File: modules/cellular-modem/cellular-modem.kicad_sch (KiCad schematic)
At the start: 20 parts, among them J1 Bus_PCI_Express_Mini, U1 TXV0108RGYR, U2 TXV0108RGYR, U3 TXV0108RGYR, U4 TPS631000DRLR, U5 TPS631000DRLR

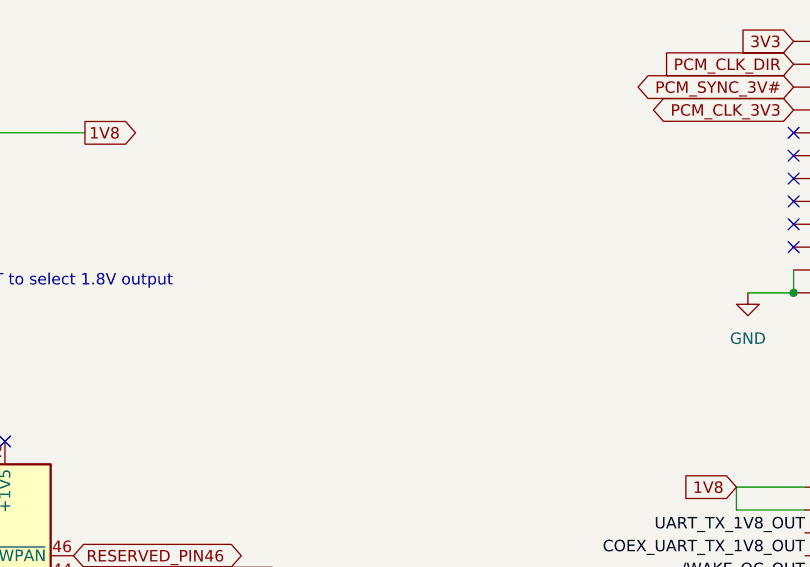
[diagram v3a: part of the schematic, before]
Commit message: add footprints etc for miniPCIe connector
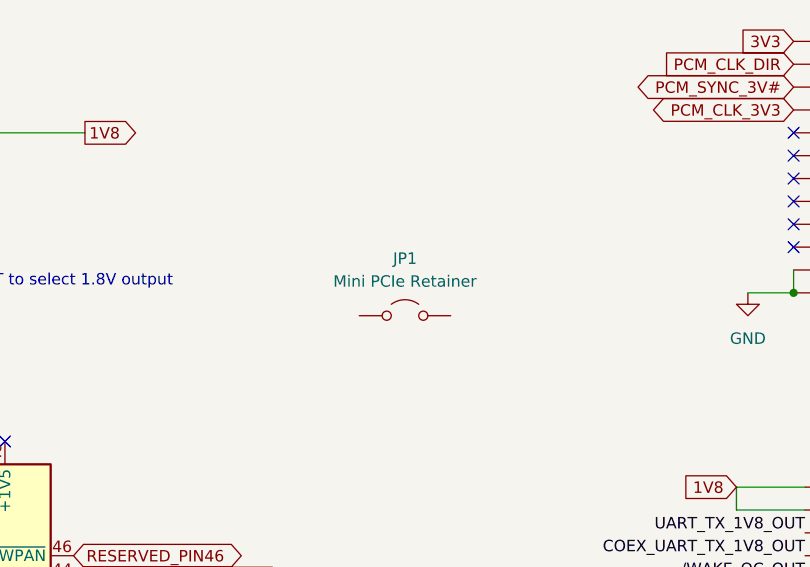
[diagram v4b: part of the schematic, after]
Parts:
- added JP1: Mini PCIe Retainer, cellular-modem:JAE_MM60-EZH059-B5-R650, symbol Jumper:Jumper_2_Open
- J1: footprint Connector_PCBEdge:BUS_PCI_Express_Mini_Dual -> cellular-modem:CONN_MM60-52B1-E1-R650_JAE
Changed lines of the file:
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@@
+	)
+	(symbol
+		(lib_id "Jumper:Jumper_2_Open")
+		(at 176.53 107.95 0)
+		(unit 1)
+		(exclude_from_sim yes)
+		(in_bom yes)
+		(on_board yes)
+		(dnp no)
+		(fields_autoplaced yes)
+		(property "Reference" "JP1"
+			(at 176.53 101.6 0)
+			(effects
+				(font
+					(size 1.27 1.27)
+				)
+			)
+		)
+		(property "Value" "Mini PCIe Retainer"
+			(at 176.53 104.14 0)
+			(effects
+				(font
+					(size 1.27 1.27)
+				)
+			)
+		)
+		(property "Footprint" "cellular-modem:JAE_MM60-EZH059-B5-R650"
+			(at 176.53 107.95 0)
+			(effects
+				(font
+					(size 1.27 1.27)
+				)
+				(hide yes)
+			)
+		)
+		(property "Datasheet" "~"
+			(at 176.53 107.95 0)
+			(effects
+				(font
+					(size 1.27 1.27)
+				)
+				(hide yes)
+			)
+		)
+		(property "Description" "Jumper, 2-pole, open"
+			(at 176.53 107.95 0)
+			(effects
+				(font
+					(size 1.27 1.27)
+				)
+				(hide yes)
+			)
+		)
+		(pin "S2"
+		)
+		(pin "S1"
+		)
+		(instances
+			(project ""
+				(path "/702a66ff-d41c-40a3-a8d1-3e4f59e31d29"
+					(reference "JP1")
+					(unit 1)
+				)
+			)
+		)
 	)
 	(symbol
@@
 			)
 		)
-		(property "Footprint" "Connector_PCBEdge:BUS_PCI_Express_Mini_Dual"
+		(property "Footprint" "cellular-modem:CONN_MM60-52B1-E1-R650_JAE"
 			(at 121.92 154.94 0)
 			(effects

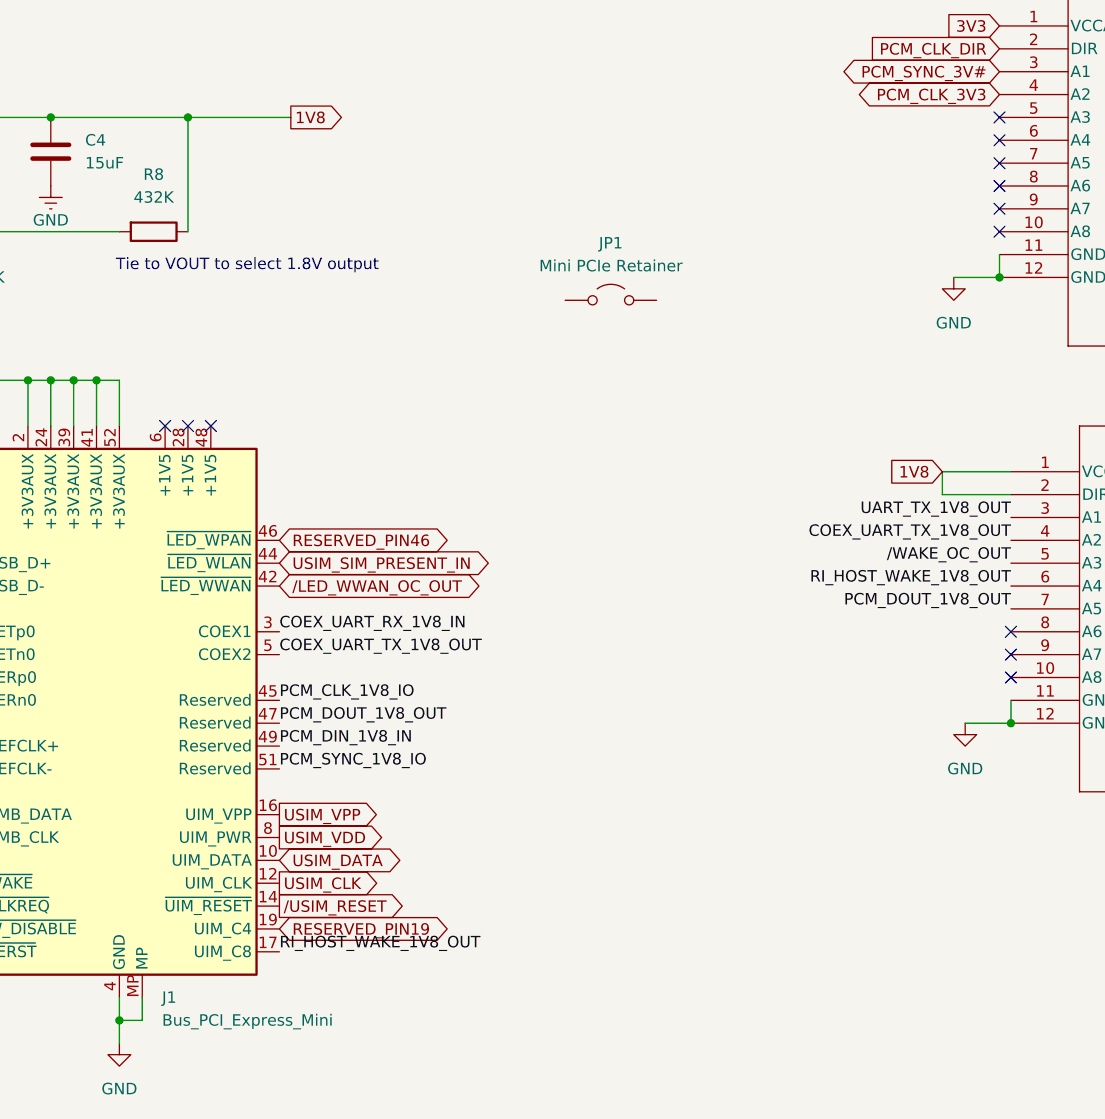
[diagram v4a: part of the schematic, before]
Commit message: switch to and place MM60 symbols and footprints
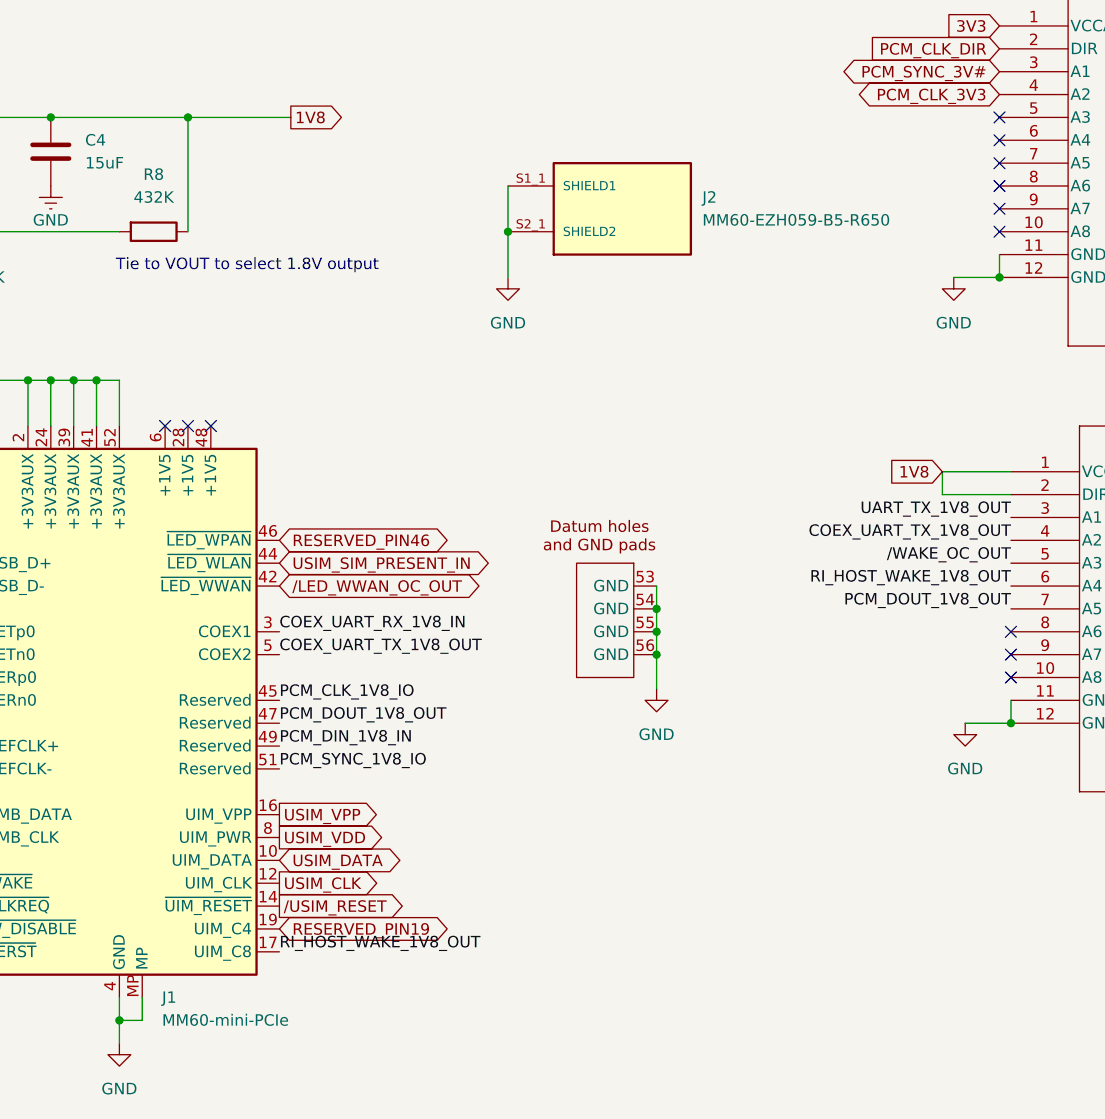
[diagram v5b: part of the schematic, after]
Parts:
- removed J1: Bus_PCI_Express_Mini, cellular-modem:CONN_MM60-52B1-E1-R650_JAE, symbol Connector:Bus_PCI_Express_Mini
- removed JP1: Mini PCIe Retainer, cellular-modem:JAE_MM60-EZH059-B5-R650, symbol Jumper:Jumper_2_Open
- added J1: MM60-mini-PCIe, cellular-modem:CONN_MM60-52B1-E1-R650_JAE, symbol MM60-EZH059-B5-R650:MM60-mini-PCIe
- added J2: MM60-EZH059-B5-R650, cellular-modem:JAE_MM60-EZH059-B5-R650, symbol MM60-EZH059-B5-R650:MM60-EZH059-B5-R650
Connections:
- net 3V3: now also J1.2 (+3V3AUX), J1.24 (+3V3AUX), J1.39 (+3V3AUX), J1.41 (+3V3AUX), J1.52 (+3V3AUX)
- net COEX_UART_RX_1V8_IN: now also J1.3 (COEX1)
- net COEX_UART_TX_1V8_OUT: now also J1.5 (COEX2)
- net GND: now also J1.15 (GND), J1.18 (GND), J1.21 (GND), J1.26 (GND), J1.27 (GND), J1.29 (GND), J1.34 (GND), J1.35 (GND), J1.37 (GND), J1.4 (GND), J1.40 (GND), J1.43 (GND), J1.50 (GND), J1.53 (GND), J1.54 (GND), J1.55 (GND), J1.56 (GND), J1.9 (GND), J1.MP, J2.S1_1 (SHIELD1), J2.S2_1 (SHIELD2)
- net I2C_DATA_1V8: now also J1.32 (SMB_DATA)
- net I2C_SCL_1V8: now also J1.30 (SMB_CLK)
- net PCM_CLK_1V8_IO: now also J1.45 (Reserved)
- net PCM_DIN_1V8_IN: now also J1.49 (Reserved)
- net PCM_DOUT_1V8_OUT: now also J1.47 (Reserved)
- net PCM_SYNC_1V8_IO: now also J1.51 (Reserved)
- net PERp0: now also J1.25 (PERp0)
- net PETp0: now also J1.33 (PETp0)
- net RESERVED_PIN19: now also J1.19 (UIM_C4)
- net RESERVED_PIN46: now also J1.46 (~{LED_WPAN})
- net RI_HOST_WAKE_1V8_OUT: now also J1.17 (UIM_C8)
- net UART_CTS_1V8_IN: now also J1.23 (PERn0)
- net UART_RX_1V8_IN: now also J1.11 (REFCLK-)
- net UART_TX_1V8_OUT: now also J1.13 (REFCLK+)
- net USB_D+: now also J1.38 (USB_D+)
- net USB_D-: now also J1.36 (USB_D-)
- net USIM_CLK: now also J1.12 (UIM_CLK)
- net USIM_DATA: now also J1.10 (UIM_DATA)
- net USIM_SIM_PRESENT_IN: now also J1.44 (~{LED_WLAN})
- net USIM_VDD: now also J1.8 (UIM_PWR)
- net USIM_VPP: now also J1.16 (UIM_VPP)
- net /CLKREQ: now also J1.7 (~{CLKREQ})
- net /DTR_SLEEP_MODE_1V8_IN: now also J1.31 (PETn0)
- net /LED_WWAN_OC_OUT: now also J1.42 (~{LED_WWAN})
- net /RESET_1V8_IN: now also J1.22 (~{PERST})
- net /USIM_RESET: now also J1.14 (~{UIM_RESET})
- net /WAKE_OC_OUT: now also J1.1 (~{WAKE})
- net /W_DISABLE_1V8_IN: now also J1.20 (~{W_DISABLE})

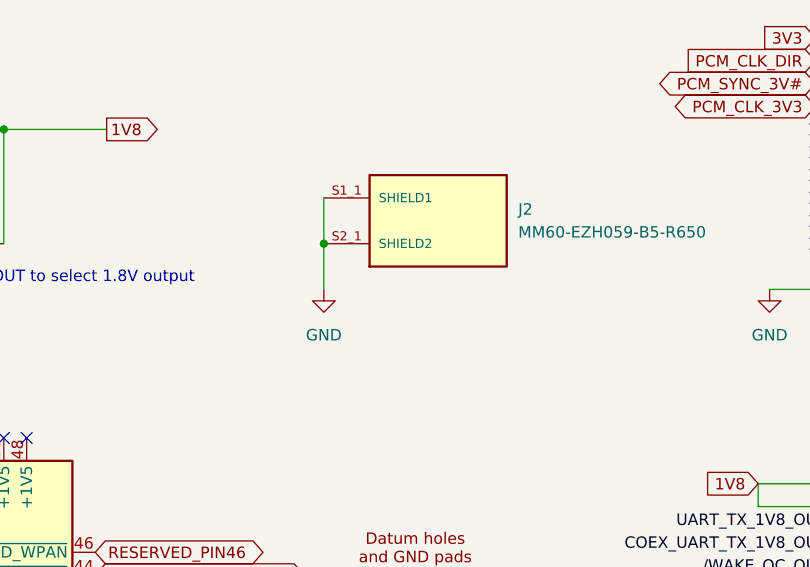
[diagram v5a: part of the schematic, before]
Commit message: add missing shield pads to MM60 retainer
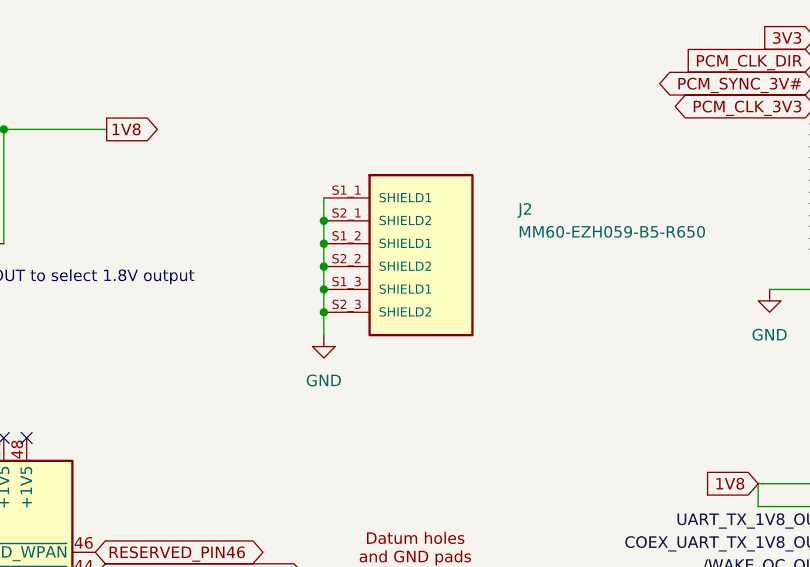
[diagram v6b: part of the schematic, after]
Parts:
- J2: footprint cellular-modem:JAE_MM60-EZH059-B5-R650 -> MM60-EZH059-B5-R650:JAE_MM60-EZH059-B5-R650
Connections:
- net GND: now also J2.S1_2 (SHIELD1), J2.S1_3 (SHIELD1), J2.S2_2 (SHIELD2), J2.S2_3 (SHIELD2)
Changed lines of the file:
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@@
 	)
 	(junction
+		(at 165.1 97.79)
+		(diameter 0)
+		(color 0 0 0 0)
+	)
+	(junction
+		(at 165.1 107.95)
+		(diameter 0)
+		(color 0 0 0 0)
+	)
+	(junction
+		(at 165.1 105.41)
+		(diameter 0)
+		(color 0 0 0 0)
+	)
+	(junction
 		(at 104.14 21.59)
 		(diameter 0)
@@
 	)
 	(junction
+		(at 165.1 102.87)
+		(diameter 0)
+		(color 0 0 0 0)
+	)
+	(junction
 		(at 219.71 57.15)
 		(diameter 0)
@@
 	(wire
 		(pts
-			(xy 219.71 54.61) (xy 219.71 57.15)
+			(xy 165.1 105.41) (xy 165.1 107.95)
 		)
 		(stroke
@@
 	(wire
 		(pts
-			(xy 213.36 129.54) (xy 213.36 127)
+			(xy 219.71 54.61) (xy 219.71 57.15)
 		)
 		(stroke
@@
 	(wire
 		(pts
-			(xy 165.1 100.33) (xy 165.1 105.41)
+			(xy 213.36 129.54) (xy 213.36 127)
 		)
 		(stroke
@@
 	(wire
 		(pts
+			(xy 165.1 97.79) (xy 165.1 100.33)
+		)
+		(stroke
+			(width 0)
+			(type default)
+		)
+	)
+	(wire
+		(pts
 			(xy 91.44 95.25) (xy 99.06 95.25)
 		)
@@
 	(wire
 		(pts
+			(xy 165.1 100.33) (xy 165.1 102.87)
+		)
+		(stroke
+			(width 0)
+			(type default)
+		)
+	)
+	(wire
+		(pts
 			(xy 181.61 142.24) (xy 181.61 144.78)
 		)
@@
 	(wire
 		(pts
-			(xy 165.1 95.25) (xy 165.1 100.33)
+			(xy 116.84 116.84) (xy 119.38 116.84)
 		)
 		(stroke
@@
 	(wire
 		(pts
-			(xy 116.84 116.84) (xy 119.38 116.84)
+			(xy 165.1 107.95) (xy 165.1 110.49)
 		)
 		(stroke
@@
 	(wire
 		(pts
+			(xy 165.1 102.87) (xy 165.1 105.41)
+		)
+		(stroke
+			(width 0)
+			(type default)
+		)
+	)
+	(wire
+		(pts
 			(xy 119.38 116.84) (xy 119.38 121.92)
 		)
@@
 	(wire
 		(pts
+			(xy 165.1 95.25) (xy 165.1 97.79)
+		)
+		(stroke
+			(width 0)
+			(type default)
+		)
+	)
+	(wire
+		(pts
 			(xy 261.62 120.65) (xy 266.7 120.65)
 		)
@@
 			)
 		)
-		(property "Footprint" "cellular-modem:JAE_MM60-EZH059-B5-R650"
+		(property "Footprint" "MM60-EZH059-B5-R650:JAE_MM60-EZH059-B5-R650"
 			(at 177.8 97.79 0)
 			(effects
@@
 		(pin "S1_1"
 		)
+		(pin "S2_3"
+		)
+		(pin "S1_3"
+		)
+		(pin "S2_2"
+		)
+		(pin "S1_2"
+		)
 		(instances
 			(project ""
@@
 	(symbol
 		(lib_id "power:GND")
-		(at 165.1 105.41 0)
+		(at 165.1 110.49 0)
 		(unit 1)
 		(exclude_from_sim no)
@@
 		(fields_autoplaced yes)
 		(property "Reference" "#PWR025"
-			(at 165.1 111.76 0)
+			(at 165.1 116.84 0)
 			(effects
 				(font
@@
 		)
 		(property "Value" "GND"
-			(at 165.1 110.49 0)
+			(at 165.1 115.57 0)
 			(effects
 				(font
@@
 		)
 		(property "Footprint" ""
-			(at 165.1 105.41 0)
+			(at 165.1 110.49 0)
 			(effects
 				(font
@@
 		)
 		(property "Datasheet" ""
-			(at 165.1 105.41 0)
+			(at 165.1 110.49 0)
 			(effects
 				(font
@@
 		)
 		(property "Description" "Power symbol creates a global label with name \"GND\" , ground"
-			(at 165.1 105.41 0)
+			(at 165.1 110.49 0)
 			(effects
 				(font

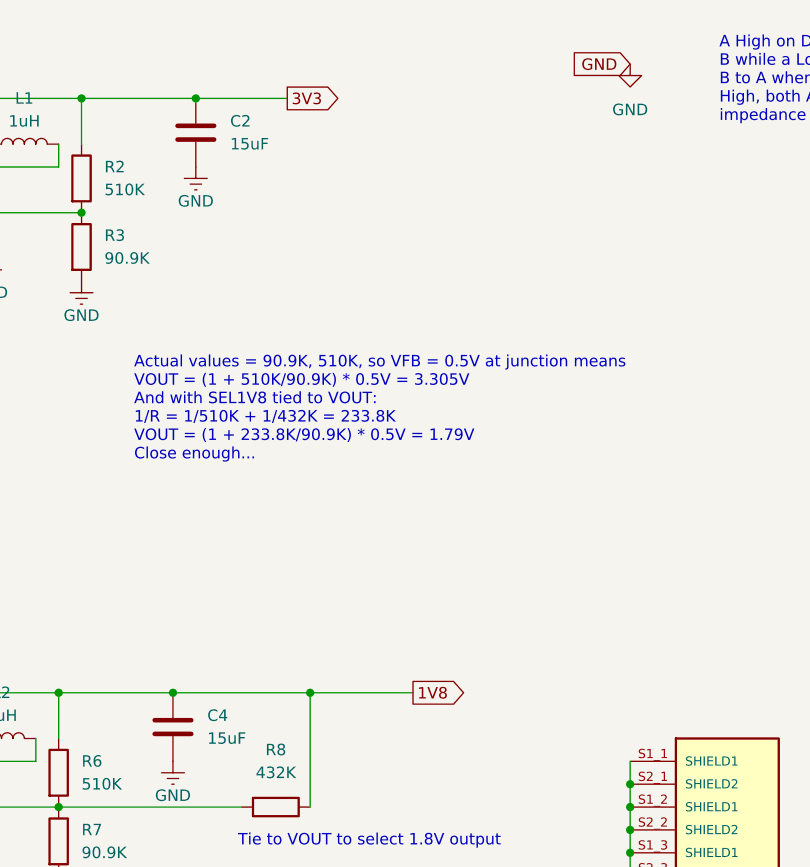
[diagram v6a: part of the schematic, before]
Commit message: add jumpers for isolating 1.8V and 3.3V regulators
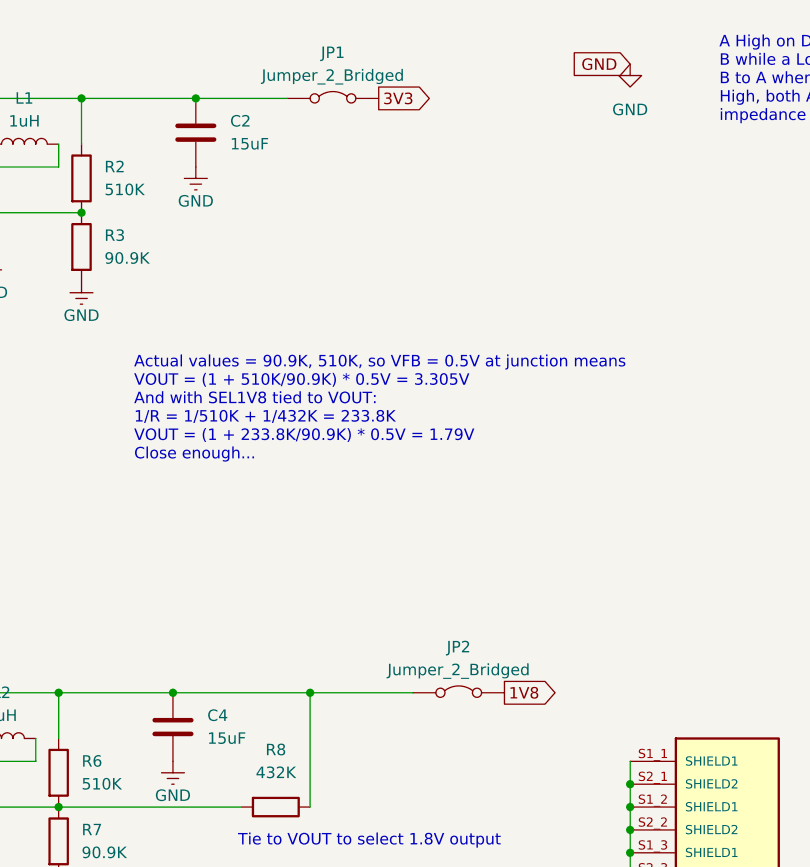
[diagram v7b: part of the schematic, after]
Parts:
- added JP1, JP2: Jumper_2_Bridged, Jumper:SolderJumper-2_P1.3mm_Bridged2Bar_RoundedPad1.0x1.5mm, symbol Jumper:Jumper_2_Bridged
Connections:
- net 1V8: now also JP2.2 (B); no longer C4.1, R6.1, R8.1, U5.1 (VOUT)
- net 3V3: now also JP1.2 (B); no longer C2.1, R2.1, U4.1 (VOUT)
- new net: C4.1, JP2.1 (A), R6.1, R8.1, U5.1 (VOUT)
- new net: C2.1, JP1.1 (A), R2.1, U4.1 (VOUT)
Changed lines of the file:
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@@
 	(global_label "1V8"
 		(shape output)
-		(at 140.97 87.63 0)
+		(at 151.13 87.63 0)
 		(fields_autoplaced yes)
 		(effects
@@
 		)
 		(property "Intersheetrefs" "${INTERSHEET_REFS}"
-			(at 147.4628 87.63 0)
+			(at 157.6228 87.63 0)
 			(effects
 				(font
@@
 	(global_label "3V3"
 		(shape output)
-		(at 127 21.59 0)
+		(at 137.16 21.59 0)
 		(fields_autoplaced yes)
 		(effects
@@
 		)
 		(property "Intersheetrefs" "${INTERSHEET_REFS}"
-			(at 133.4928 21.59 0)
+			(at 143.6528 21.59 0)
 			(effects
 				(font
@@
 	)
 	(symbol
+		(lib_id "Jumper:Jumper_2_Bridged")
+		(at 132.08 21.59 0)
+		(unit 1)
+		(exclude_from_sim yes)
+		(in_bom yes)
+		(on_board yes)
+		(dnp no)
+		(fields_autoplaced yes)
+		(property "Reference" "JP1"
+			(at 132.08 16.51 0)
+			(effects
+				(font
+					(size 1.27 1.27)
+				)
+			)
+		)
+		(property "Value" "Jumper_2_Bridged"
+			(at 132.08 19.05 0)
+			(effects
+				(font
+					(size 1.27 1.27)
+				)
+			)
+		)
+		(property "Footprint" "Jumper:SolderJumper-2_P1.3mm_Bridged2Bar_RoundedPad1.0x1.5mm"
+			(at 132.08 21.59 0)
+			(effects
+				(font
+					(size 1.27 1.27)
+				)
+				(hide yes)
+			)
+		)
+		(property "Datasheet" "~"
+			(at 132.08 21.59 0)
+			(effects
+				(font
+					(size 1.27 1.27)
+				)
+				(hide yes)
+			)
+		)
+		(property "Description" "Jumper, 2-pole, closed/bridged"
+			(at 132.08 21.59 0)
+			(effects
+				(font
+					(size 1.27 1.27)
+				)
+				(hide yes)
+			)
+		)
+		(pin "1"
+		)
+		(pin "2"
+		)
+		(instances
+			(project ""
+				(path "/702a66ff-d41c-40a3-a8d1-3e4f59e31d29"
+					(reference "JP1")
+					(unit 1)
+				)
+			)
+		)
+	)
+	(symbol
 		(lib_id "power:Earth")
 		(at 93.98 39.37 0)
@@
 					(unit 1)
 				)
+			)
+		)
+	)
+	(symbol
+		(lib_id "Jumper:Jumper_2_Bridged")
+		(at 146.05 87.63 0)
+		(unit 1)
+		(exclude_from_sim yes)
+		(in_bom yes)
+		(on_board yes)
+		(dnp no)
+		(fields_autoplaced yes)
+		(property "Reference" "JP2"
+			(at 146.05 82.55 0)
+			(effects
+				(font
+					(size 1.27 1.27)
+				)
+			)
+		)
+		(property "Value" "Jumper_2_Bridged"
+			(at 146.05 85.09 0)
+			(effects
+				(font
+					(size 1.27 1.27)
+				)
+			)
+		)
+		(property "Footprint" "Jumper:SolderJumper-2_P1.3mm_Bridged2Bar_RoundedPad1.0x1.5mm"
+			(at 146.05 87.63 0)
+			(effects
+				(font
+					(size 1.27 1.27)
+				)
+				(hide yes)
+			)
+		)
+		(property "Datasheet" "~"
+			(at 146.05 87.63 0)
+			(effects
+				(font
+					(size 1.27 1.27)
+				)
+				(hide yes)
+			)
+		)
+		(property "Description" "Jumper, 2-pole, closed/bridged"
+			(at 146.05 87.63 0)
+			(effects
+				(font
+					(size 1.27 1.27)
+				)
+				(hide yes)
+			)
+		)
+		(pin "1"
+		)
+		(pin "2"
+		)
+		(instances
+			(project "cellular-modem"
+				(path "/702a66ff-d41c-40a3-a8d1-3e4f59e31d29"
+					(reference "JP2")
+					(unit 1)
+				)
